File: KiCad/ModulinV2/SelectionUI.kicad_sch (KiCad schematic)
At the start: 24 parts, among them IC34 E-ULN2003D1013TR, IC35 E-ULN2003D1013TR, IC36 CD4028BM96, IC37 CD4028BM96

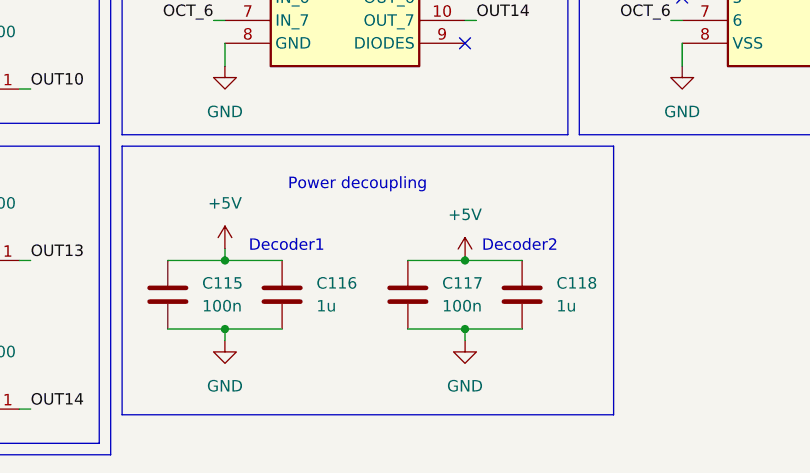
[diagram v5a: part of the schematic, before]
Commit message: Completed tuning & mod wheel layouts
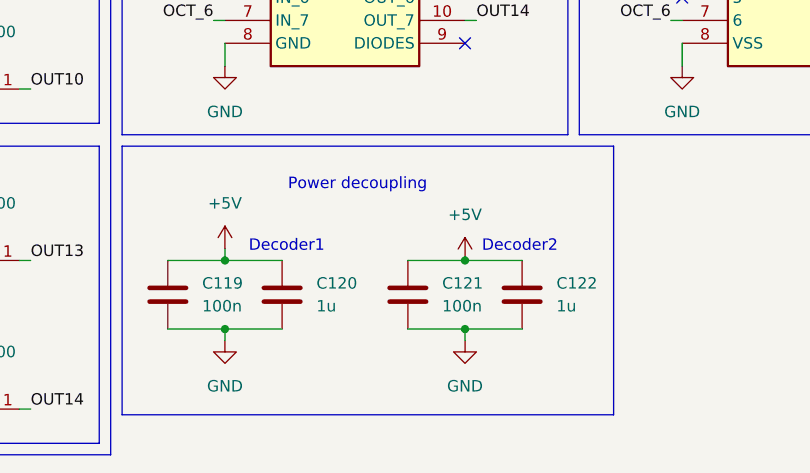
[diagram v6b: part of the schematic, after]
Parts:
- renumbered C115 to C119, C116 to C120, C117 to C121, C118 to C122
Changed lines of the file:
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@@
 		(dnp no)
 		(fields_autoplaced yes)
-		(property "Reference" "#PWR0258"
+		(property "Reference" "#PWR0261"
 			(at 186.69 153.67 0)
 			(effects
@@
 			(project "ModulinV2"
 				(path "/c6b34a57-3941-4b56-8b80-1848c7f41082/ba5ade70-a939-4914-9429-1ad400c74d73/e799dfb0-018d-4a0c-90e3-bc5a892eb818"
-					(reference "#PWR0258")
+					(reference "#PWR0261")
 					(unit 1)
 				)
@@
 		(dnp no)
 		(fields_autoplaced yes)
-		(property "Reference" "#PWR0254"
+		(property "Reference" "#PWR0257"
 			(at 160.02 123.19 0)
 			(effects
@@
 			(project "ModulinV2"
 				(path "/c6b34a57-3941-4b56-8b80-1848c7f41082/ba5ade70-a939-4914-9429-1ad400c74d73/e799dfb0-018d-4a0c-90e3-bc5a892eb818"
-					(reference "#PWR0254")
+					(reference "#PWR0257")
 					(unit 1)
 				)
@@
 		(dnp no)
 		(fields_autoplaced yes)
-		(property "Reference" "#PWR0260"
+		(property "Reference" "#PWR0263"
 			(at 210.82 123.19 0)
 			(effects
@@
 			(project "ModulinV2"
 				(path "/c6b34a57-3941-4b56-8b80-1848c7f41082/ba5ade70-a939-4914-9429-1ad400c74d73/e799dfb0-018d-4a0c-90e3-bc5a892eb818"
-					(reference "#PWR0260")
+					(reference "#PWR0263")
 					(unit 1)
 				)
@@
 		(dnp no)
 		(fields_autoplaced yes)
-		(property "Reference" "#PWR0253"
+		(property "Reference" "#PWR0256"
 			(at 160.02 78.74 0)
 			(effects
@@
 			(project ""
 				(path "/c6b34a57-3941-4b56-8b80-1848c7f41082/ba5ade70-a939-4914-9429-1ad400c74d73/e799dfb0-018d-4a0c-90e3-bc5a892eb818"
-					(reference "#PWR0253")
+					(reference "#PWR0256")
 					(unit 1)
 				)
@@
 		(dnp no)
 		(fields_autoplaced yes)
-		(property "Reference" "#PWR0251"
+		(property "Reference" "#PWR0254"
 			(at 52.07 52.07 0)
 			(effects
@@
 			(project ""
 				(path "/c6b34a57-3941-4b56-8b80-1848c7f41082/ba5ade70-a939-4914-9429-1ad400c74d73/e799dfb0-018d-4a0c-90e3-bc5a892eb818"
-					(reference "#PWR0251")
+					(reference "#PWR0254")
 					(unit 1)
 				)
@@
 		(dnp no)
 		(fields_autoplaced yes)
-		(property "Reference" "#PWR0252"
+		(property "Reference" "#PWR0255"
 			(at 52.07 120.65 0)
 			(effects
@@
 			(project "ModulinV2"
 				(path "/c6b34a57-3941-4b56-8b80-1848c7f41082/ba5ade70-a939-4914-9429-1ad400c74d73/e799dfb0-018d-4a0c-90e3-bc5a892eb818"
-					(reference "#PWR0252")
+					(reference "#PWR0255")
 					(unit 1)
 				)
@@
 		(dnp no)
 		(fields_autoplaced yes)
-		(property "Reference" "#PWR0259"
+		(property "Reference" "#PWR0262"
 			(at 210.82 78.74 0)
 			(effects
@@
 			(project "ModulinV2"
 				(path "/c6b34a57-3941-4b56-8b80-1848c7f41082/ba5ade70-a939-4914-9429-1ad400c74d73/e799dfb0-018d-4a0c-90e3-bc5a892eb818"
-					(reference "#PWR0259")
+					(reference "#PWR0262")
 					(unit 1)
 				)
@@
 		(dnp no)
 		(fields_autoplaced yes)
-		(property "Reference" "C115"
+		(property "Reference" "C119"
 			(at 157.48 140.9699 0)
 			(effects
@@
 			(project "ModulinV2"
 				(path "/c6b34a57-3941-4b56-8b80-1848c7f41082/ba5ade70-a939-4914-9429-1ad400c74d73/e799dfb0-018d-4a0c-90e3-bc5a892eb818"
-					(reference "C115")
+					(reference "C119")
 					(unit 1)
 				)
@@
 		(dnp no)
 		(fields_autoplaced yes)
-		(property "Reference" "#PWR0255"
+		(property "Reference" "#PWR0258"
 			(at 160.02 140.97 0)
 			(effects
@@
 			(project "ModulinV2"
 				(path "/c6b34a57-3941-4b56-8b80-1848c7f41082/ba5ade70-a939-4914-9429-1ad400c74d73/e799dfb0-018d-4a0c-90e3-bc5a892eb818"
-					(reference "#PWR0255")
+					(reference "#PWR0258")
 					(unit 1)
 				)
@@
 		(dnp no)
 		(fields_autoplaced yes)
-		(property "Reference" "C116"
+		(property "Reference" "C120"
 			(at 170.18 140.9699 0)
 			(effects
@@
 			(project "ModulinV2"
 				(path "/c6b34a57-3941-4b56-8b80-1848c7f41082/ba5ade70-a939-4914-9429-1ad400c74d73/e799dfb0-018d-4a0c-90e3-bc5a892eb818"
-					(reference "C116")
+					(reference "C120")
 					(unit 1)
 				)
@@
 		(dnp no)
 		(fields_autoplaced yes)
-		(property "Reference" "#PWR0262"
+		(property "Reference" "#PWR0265"
 			(at 236.22 97.79 0)
 			(effects
@@
 			(project "ModulinV2"
 				(path "/c6b34a57-3941-4b56-8b80-1848c7f41082/ba5ade70-a939-4914-9429-1ad400c74d73/e799dfb0-018d-4a0c-90e3-bc5a892eb818"
-					(reference "#PWR0262")
+					(reference "#PWR0265")
 					(unit 1)
 				)
@@
 		(dnp no)
 		(fields_autoplaced yes)
-		(property "Reference" "#PWR0261"
+		(property "Reference" "#PWR0264"
 			(at 236.22 53.34 0)
 			(effects
@@
 			(project "ModulinV2"
 				(path "/c6b34a57-3941-4b56-8b80-1848c7f41082/ba5ade70-a939-4914-9429-1ad400c74d73/e799dfb0-018d-4a0c-90e3-bc5a892eb818"
-					(reference "#PWR0261")
+					(reference "#PWR0264")
 					(unit 1)
 				)
@@
 		(dnp no)
 		(fields_autoplaced yes)
-		(property "Reference" "C117"
+		(property "Reference" "C121"
 			(at 184.15 140.9699 0)
 			(effects
@@
 			(project "ModulinV2"
 				(path "/c6b34a57-3941-4b56-8b80-1848c7f41082/ba5ade70-a939-4914-9429-1ad400c74d73/e799dfb0-018d-4a0c-90e3-bc5a892eb818"
-					(reference "C117")
+					(reference "C121")
 					(unit 1)
 				)
@@
 		(dnp no)
 		(fields_autoplaced yes)
-		(property "Reference" "#PWR0263"
+		(property "Reference" "#PWR0266"
 			(at 246.38 115.57 0)
 			(effects
@@
 			(project "ModulinV2"
 				(path "/c6b34a57-3941-4b56-8b80-1848c7f41082/ba5ade70-a939-4914-9429-1ad400c74d73/e799dfb0-018d-4a0c-90e3-bc5a892eb818"
-					(reference "#PWR0263")
+					(reference "#PWR0266")
 					(unit 1)
 				)
@@
 		(dnp no)
 		(fields_autoplaced yes)
-		(property "Reference" "#PWR0256"
+		(property "Reference" "#PWR0259"
 			(at 160.02 153.67 0)
 			(effects
@@
 			(project "ModulinV2"
 				(path "/c6b34a57-3941-4b56-8b80-1848c7f41082/ba5ade70-a939-4914-9429-1ad400c74d73/e799dfb0-018d-4a0c-90e3-bc5a892eb818"
-					(reference "#PWR0256")
+					(reference "#PWR0259")
 					(unit 1)
 				)
@@
 		(dnp no)
 		(fields_autoplaced yes)
-		(property "Reference" "#PWR0257"
+		(property "Reference" "#PWR0260"
 			(at 186.69 142.24 0)
 			(effects
@@
 			(project "ModulinV2"
 				(path "/c6b34a57-3941-4b56-8b80-1848c7f41082/ba5ade70-a939-4914-9429-1ad400c74d73/e799dfb0-018d-4a0c-90e3-bc5a892eb818"
-					(reference "#PWR0257")
+					(reference "#PWR0260")
 					(unit 1)
 				)
@@
 		(dnp no)
 		(fields_autoplaced yes)
-		(property "Reference" "C118"
+		(property "Reference" "C122"
 			(at 196.85 140.9699 0)
 			(effects
@@
 			(project "ModulinV2"
 				(path "/c6b34a57-3941-4b56-8b80-1848c7f41082/ba5ade70-a939-4914-9429-1ad400c74d73/e799dfb0-018d-4a0c-90e3-bc5a892eb818"
-					(reference "C118")
+					(reference "C122")
 					(unit 1)
 				)

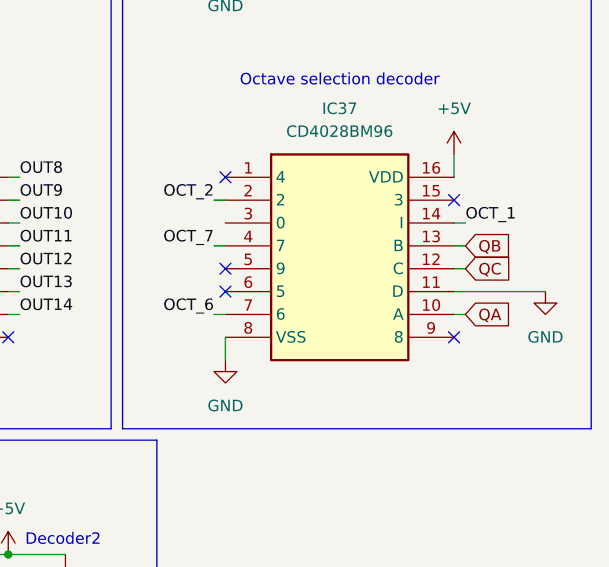
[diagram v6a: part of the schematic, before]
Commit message: FInished LFO, octave/wave selector and UI layout
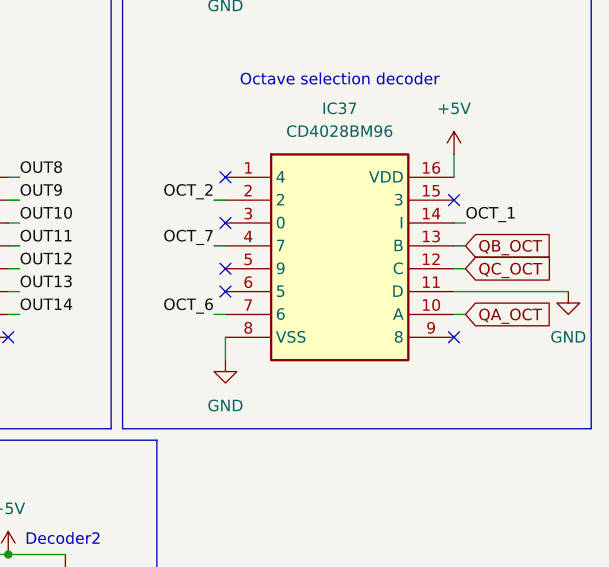
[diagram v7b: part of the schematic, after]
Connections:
- net QA: no longer IC37.10 (A)
- net QB: no longer IC37.13 (B)
- net QC: no longer IC37.12 (C)
- new net QA_OCT: IC37.10 (A)
- new net QB_OCT: IC37.13 (B)
- new net QC_OCT: IC37.12 (C)
- no-connect marks 11 -> 12
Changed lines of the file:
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@@
 	)
 	(no_connect
+		(at 210.82 101.6)
+	)
+	(no_connect
 		(at 54.61 129.54)
 	)
@@
 	(wire
 		(pts
-			(xy 236.22 109.22) (xy 246.38 109.22)
+			(xy 236.22 109.22) (xy 248.92 109.22)
 		)
 		(stroke
@@
 		)
 	)
-	(global_label "QA"
+	(global_label "QA_OCT"
 		(shape input)
 		(at 237.49 111.76 0)
@@
 		)
 		(property "Intersheetrefs" "${INTERSHEET_REFS}"
-			(at 242.8943 111.76 0)
+			(at 247.43 111.76 0)
 			(effects
 				(font
@@
 		)
 	)
-	(global_label "QC"
+	(global_label "QC_OCT"
 		(shape input)
 		(at 237.49 106.68 0)
@@
 		)
 		(property "Intersheetrefs" "${INTERSHEET_REFS}"
-			(at 243.0757 106.68 0)
+			(at 247.6114 106.68 0)
 			(effects
 				(font
@@
 		)
 	)
-	(global_label "QB"
+	(global_label "QB_OCT"
 		(shape input)
 		(at 237.49 104.14 0)
@@
 		)
 		(property "Intersheetrefs" "${INTERSHEET_REFS}"
-			(at 243.0757 104.14 0)
+			(at 247.6114 104.14 0)
 			(effects
 				(font
@@
 	(symbol
 		(lib_id "power:GND")
-		(at 246.38 109.22 0)
+		(at 248.92 109.22 0)
 		(unit 1)
 		(exclude_from_sim no)
@@
 		(fields_autoplaced yes)
 		(property "Reference" "#PWR0266"
-			(at 246.38 115.57 0)
+			(at 248.92 115.57 0)
 			(effects
 				(font
@@
 		)
 		(property "Value" "GND"
-			(at 246.38 114.3 0)
+			(at 248.92 114.3 0)
 			(effects
 				(font
@@
 		)
 		(property "Footprint" ""
-			(at 246.38 109.22 0)
+			(at 248.92 109.22 0)
 			(effects
 				(font
@@
 		)
 		(property "Datasheet" ""
-			(at 246.38 109.22 0)
+			(at 248.92 109.22 0)
 			(effects
 				(font
@@
 		)
 		(property "Description" "Power symbol creates a global label with name \"GND\" , ground"
-			(at 246.38 109.22 0)
+			(at 248.92 109.22 0)
 			(effects
 				(font

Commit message: Fixed schematic connections
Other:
- company: (none) -> TalTech
- title: (none) -> Selection UI
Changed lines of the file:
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@@
 	(paper "A4")
 	(title_block
+		(title "Selection UI")
+		(date "2026-04-29")
+		(rev "1.4")
+		(company "TalTech")
 		(comment 1 "Instructor: Kaiser Pärnamets")
-		(comment 2 "By: Rasmus Palk")
+		(comment 2 "Author: Rasmus Palk")
 	)
 	(rectangle
